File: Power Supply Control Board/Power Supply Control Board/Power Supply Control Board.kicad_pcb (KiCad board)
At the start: 2 copper layers, 50.8 x 46 mm, 50 parts, among them J1 Conn_01x12, Q1 BC546, Q2 BC546, Q3 MPSA92, Q4 BC546, U1 IR2153, U2 LM311, U3 LM311

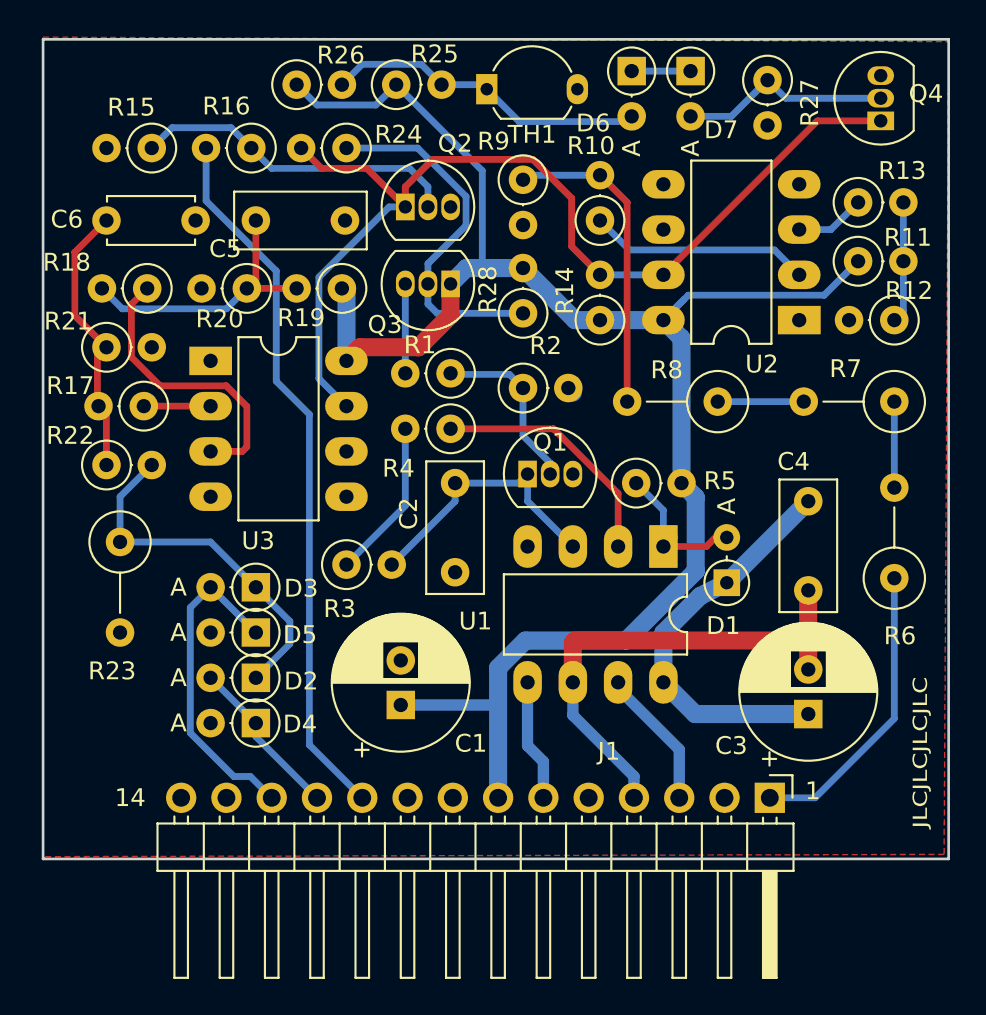
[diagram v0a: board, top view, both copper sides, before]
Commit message: Add Top Layer Zones and some graphics to Main Board V2.0
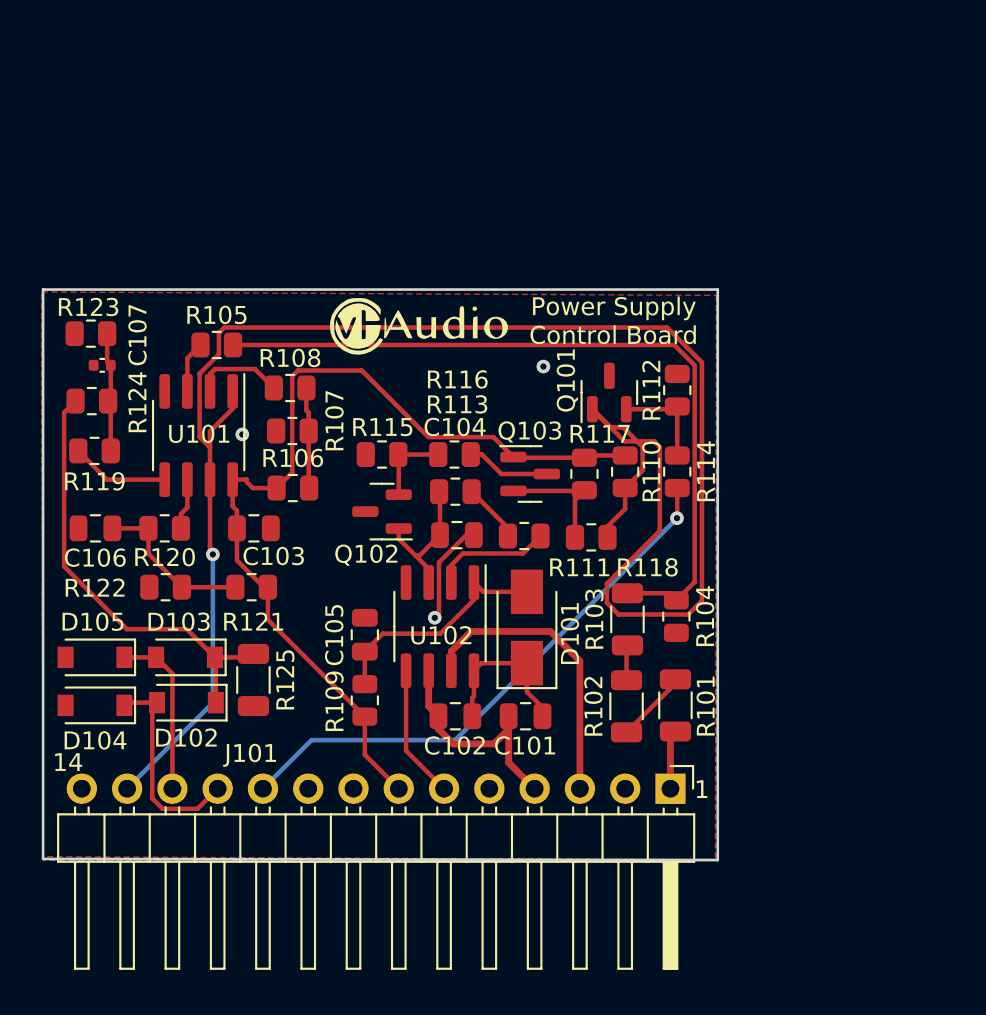
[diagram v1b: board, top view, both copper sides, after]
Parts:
- removed C1, C3: 33µ/25V, Capacitor_THT:CP_Radial_D7.5mm_P2.50mm
- removed C2: 4n7, Capacitor_THT:C_Rect_L7.2mm_W3.0mm_P5.00mm_FKS2_FKP2_MKS2_MKP2
- removed C4: 10n, Capacitor_THT:C_Rect_L7.2mm_W3.0mm_P5.00mm_FKS2_FKP2_MKS2_MKP2
- removed C5: 100n, Capacitor_THT:C_Rect_L7.2mm_W3.0mm_P5.00mm_FKS2_FKP2_MKS2_MKP2
- removed C6: 47p, Capacitor_THT:C_Disc_D4.7mm_W2.5mm_P5.00mm
- removed D1: MUR140, Diode_THT:D_DO-34_SOD68_P2.54mm_Vertical_AnodeUp
- removed D2, D3, D4, D5, D6: 1N4148, Diode_THT:D_DO-35_SOD27_P2.54mm_Vertical_AnodeUp
- removed D7: BZX55C4V7, Diode_THT:D_DO-35_SOD27_P2.54mm_Vertical_AnodeUp
- removed J1: Conn_01x12, Connector_PinHeader_2.54mm:PinHeader_1x14_P2.54mm_Horizontal
- removed Q1, Q2, Q4: BC546, Package_TO_SOT_THT:TO-92_Inline
- removed Q3: MPSA92, Package_TO_SOT_THT:TO-92_Inline
- removed R1, R15, R16, R17, R18, R2, R20, R28: 10k, Resistor_THT:R_Axial_DIN0207_L6.3mm_D2.5mm_P2.54mm_Vertical
- removed R10, R12, R13: 47k, Resistor_THT:R_Axial_DIN0207_L6.3mm_D2.5mm_P2.54mm_Vertical
- removed R11: 56k, Resistor_THT:R_Axial_DIN0207_L6.3mm_D2.5mm_P2.54mm_Vertical
- removed R14: 5k6, Resistor_THT:R_Axial_DIN0207_L6.3mm_D2.5mm_P2.54mm_Vertical
- removed R19: 82k, Resistor_THT:R_Axial_DIN0207_L6.3mm_D2.5mm_P2.54mm_Vertical
- removed R21: 22k, Resistor_THT:R_Axial_DIN0207_L6.3mm_D2.5mm_P2.54mm_Vertical
- removed R22, R24, R27, R9: 12k, Resistor_THT:R_Axial_DIN0207_L6.3mm_D2.5mm_P2.54mm_Vertical
- removed R23: 22 0,5W, Resistor_THT:R_Axial_DIN0309_L9.0mm_D3.2mm_P5.08mm_Vertical
- removed R25: 3k9, Resistor_THT:R_Axial_DIN0207_L6.3mm_D2.5mm_P2.54mm_Vertical
- removed R26: 33k, Resistor_THT:R_Axial_DIN0207_L6.3mm_D2.5mm_P2.54mm_Vertical
- removed R3, R4: 1k, Resistor_THT:R_Axial_DIN0207_L6.3mm_D2.5mm_P2.54mm_Vertical
- removed R5: 150, Resistor_THT:R_Axial_DIN0207_L6.3mm_D2.5mm_P2.54mm_Vertical
- removed R6, R7, R8: 150k 0.5W, Resistor_THT:R_Axial_DIN0309_L9.0mm_D3.2mm_P5.08mm_Vertical
- removed TH1: KTY81-110, Package_TO_SOT_THT:SOD-70_P5.08mm
- removed U1: IR2153, Package_DIP:DIP-8_W7.62mm_LongPads
- removed U2, U3: LM311, Package_DIP:DIP-8_W7.62mm_LongPads
- added C101: 100n, Capacitor_SMD:C_0805_2012Metric, F.Cu at (125.9, 130.7)
- added C102: 10µ/25V, Capacitor_SMD:C_0805_2012Metric, F.Cu at (121.9, 130.7)
- added C103: 100n, Capacitor_SMD:C_0805_2012Metric, F.Cu at (110.6, 120.2)
- added C104: 4n7, Capacitor_SMD:C_0805_2012Metric, F.Cu at (122.0, 120.6)
- added C105: 10µ/25V, Capacitor_SMD:C_0805_2012Metric, F.Cu at (116.9, 126.2)
- added C106: 100n, Capacitor_SMD:C_0805_2012Metric, F.Cu at (101.7, 120.2)
- added C107: 47p, Capacitor_SMD:C_0402_1005Metric, F.Cu at (102.1, 111.1)
- added D101: US1MG, Diode_SMD:D_SMA, F.Cu at (125.9, 125.8)
- added D102: 1N4148, Diode_SMD:D_SOD-123, F.Cu at (106.8, 130.0)
- added D103: 1N4148, Diode_SMD:D_SOD-123, F.Cu at (106.8, 127.4)
- added D104: 1N4148, Diode_SMD:D_SOD-123, F.Cu at (101.7, 130.1)
- added D105: 1N4148, Diode_SMD:D_SOD-123, F.Cu at (101.7, 127.4)
- added J101: Conn_01x12, Connector_PinHeader_2.54mm:PinHeader_1x14_P2.54mm_Horizontal, F.Cu at (134.0, 134.8)
- added Q101: MMBT5551L, Package_TO_SOT_SMD:SOT-23, F.Cu at (130.6, 112.6)
- added Q102: MMBT5551L, Package_TO_SOT_SMD:SOT-23, F.Cu at (117.8, 119.3)
- added Q103: MMBT5401, Package_TO_SOT_SMD:SOT-23, F.Cu at (126.1, 117.2)
- added R101: 100k 0.5W, Resistor_SMD:R_1206_3216Metric, F.Cu at (134.3, 130.1)
- added R102: 100k 0.5W, Resistor_SMD:R_1206_3216Metric, F.Cu at (131.5, 130.2)
- added R103: 100k 0.5W, Resistor_SMD:R_1206_3216Metric, F.Cu at (131.6, 125.3)
- added R104: 2k7, Resistor_SMD:R_0805_2012Metric, F.Cu at (134.3, 125.2)
- added R105: 47k, Resistor_SMD:R_0805_2012Metric, F.Cu at (108.6, 109.9)
- added R106: 56k, Resistor_SMD:R_0805_2012Metric, F.Cu at (112.8, 117.9)
- added R107: 10k, Resistor_SMD:R_0805_2012Metric, F.Cu at (112.8, 114.7)
- added R108: 47k, Resistor_SMD:R_0805_2012Metric, F.Cu at (112.7, 112.3)
- added R109: 150, Resistor_SMD:R_0805_2012Metric, F.Cu at (116.9, 129.9)
- added R110: 5k6, Resistor_SMD:R_0805_2012Metric, F.Cu at (131.5, 117.0)
- added R111: 1k, Resistor_SMD:R_0805_2012Metric, F.Cu at (125.8, 120.6)
- added R112: 10k, Resistor_SMD:R_0805_2012Metric, F.Cu at (134.4, 112.5)
- added R113: 1k, Resistor_SMD:R_0805_2012Metric, F.Cu at (121.9, 118.1)
- added R114: 10k, Resistor_SMD:R_0805_2012Metric, F.Cu at (134.4, 117.0)
- added R115: 10k, Resistor_SMD:R_0805_2012Metric, F.Cu at (117.8, 116.1)
- added R116: 10k, Resistor_SMD:R_0805_2012Metric, F.Cu at (121.9, 116.1)
- added R117: 10k, Resistor_SMD:R_0805_2012Metric, F.Cu at (129.2, 117.2)
- added R118: 12k, Resistor_SMD:R_0805_2012Metric, F.Cu at (129.6, 120.7)
- added R119: 10k, Resistor_SMD:R_0805_2012Metric, F.Cu at (101.7, 115.9)
- added R120: 10k, Resistor_SMD:R_0805_2012Metric, F.Cu at (105.6, 120.2)
- added R121: 56k, Resistor_SMD:R_0805_2012Metric, F.Cu at (110.5, 123.5)
- added R122: 12k, Resistor_SMD:R_0805_2012Metric, F.Cu at (105.7, 123.5)
- added R123: 470k, Resistor_SMD:R_0805_2012Metric, F.Cu at (101.5, 109.3)
- added R124: 12k, Resistor_SMD:R_0805_2012Metric, F.Cu at (101.5, 113.1)
- added R125: 22 0,5W, Resistor_SMD:R_1206_3216Metric, F.Cu at (110.6, 128.7)
- added REF**: VHAudio_Logo_10mm, LogoLibrary:VHAudio_Logo_10mm, F.Cu at (119.9, 108.8)
- added U101: LM393, Package_SO:SOIC-8_3.9x4.9mm_P1.27mm, F.Cu at (107.5, 115.0)
- added U102: IR2153, Package_SO:SOIC-8_3.9x4.9mm_P1.27mm, F.Cu at (121.1, 125.7)
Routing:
- net ~ShutDown: track 0.00 -> 103.5 mm, vias 0 -> 1
- net Net-(Q2-Pad1): track 57.8 -> 0.00 mm
- net +16V: track 100.7 -> 51.6 mm
- net Net-(R103-Pad2): track 0.00 -> 42.9 mm
- net Net-(D102-Pad1): track 0.00 -> 24.9 mm
- net Net-(C3-Pad1): track 22.7 -> 0.00 mm
- net Net-(D2-Pad1): track 20.6 -> 0.00 mm
- net Net-(Q3-Pad2): track 20.3 -> 0.00 mm
- net Net-(Q2-Pad2): track 18.5 -> 0.00 mm
- net Net-(D6-Pad2): track 18.2 -> 0.00 mm
- net Net-(R10-Pad2): track 17.8 -> 0.00 mm
- net Net-(R18-Pad1): track 16.3 -> 0.00 mm
- net Net-(C5-Pad1): track 15.9 -> 0.00 mm
- net Net-(C6-Pad1): track 15.6 -> 0.00 mm
- net Net-(C2-Pad1): track 15.4 -> 0.00 mm
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- added copper zone on B.Cu, net GND
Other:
- board size 50.8 x 46 mm -> 37.8 x 32 mm
- board text added: "+16"
- board text added: "CS+"
- board text added: "CS-"
- board text added: "GND"
- board text added: "Ho"
- board text added: "Lo"
- board text added: "Power Supply Control Board"
- board text added: "SHD"
- board text added: "VB+"
- board text added: "Vs"
- board text added: "X"
- board text added: "~SHD"
